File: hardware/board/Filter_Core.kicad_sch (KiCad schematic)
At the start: 53 parts

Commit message: Updated Prototype Tests
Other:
- note removed: "Notes:"
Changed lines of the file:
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@@
-    (effects (font (size 5 5) (thickness 0.508) bold) (justify left bottom))
-  )
-  (text "Notes:" (at 21.59 180.34 0)
     (effects (font (size 5 5) (thickness 0.508) bold) (justify left bottom))
   )

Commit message: hardware: add MPNs, DigiKey part numbers, and LCSC part numbers for all BOM items
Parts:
- C? (x7): DigiKey (none) -> 490-GCM1885C2A102FA16DCT-ND; LCSC (none) -> C2219251; MPN (none) -> GCM1885C2A102FA16D; Substitutes Allowed (none) -> Ask
- C? (x3): DigiKey (none) -> 1276-1008-1-ND; LCSC (none) -> C14858; MPN (none) -> CL10C101JB8NNNC; Rating 25V/10% -> 25V/10%/C0G; Substitutes Allowed (none) -> Yes
- D? (x12): DigiKey (none) -> 1727-4309-2-ND; LCSC (none) -> C109218; Substitutes Allowed (none) -> No
- R? (x7): DigiKey (none) -> YAG1582CT-ND; LCSC (none) -> C723637; MPN (none) -> RT0603BRD0720KL; Substitutes Allowed (none) -> Ask
- R? (x3): DigiKey (none) -> YAG2323TR-ND; LCSC (none) -> C375503; MPN (none) -> RT0603FRE071KL; Substitutes Allowed (none) -> Yes
- R?: DigiKey (none) -> YAG5959CT-ND; LCSC (none) -> C706162; MPN (none) -> RT0603FRE0733KL; Substitutes Allowed (none) -> Yes
- R?: DigiKey (none) -> 13-RT0603FRE13100KLTR-ND; LCSC (none) -> C4107493; MPN (none) -> RT0603FRE13100KL; Rating 100mW/1% -> 100mW/1%/Thin; Substitutes Allowed (none) -> Yes
- R?: DigiKey (none) -> 13-RT0603FRE07330KLCT-ND; LCSC (none) -> C863745; MPN (none) -> RT0603FRE07330KL; Rating 100mW/1% -> 100mW/1%/Thin; Substitutes Allowed (none) -> Yes
- R?: DigiKey (none) -> YAG5961CT-ND; LCSC (none) -> C863790; MPN (none) -> RT0603FRE073K9L; Substitutes Allowed (none) -> Yes
- R?: DigiKey (none) -> YAG1582CT-ND; LCSC (none) -> C723637; MPN (none) -> RT0603BRD0720KL; Rating 100mW/1%/Thin -> 100mW/0.1%/Thin; Substitutes Allowed (none) -> Ask
- R?: DigiKey (none) -> 13-RT0603FRE071K8LCT-ND; LCSC (none) -> C375505; MPN (none) -> RT0603FRE071K8L; Rating 100mW/1% -> 100mW/1%/Thin; Substitutes Allowed (none) -> Yes
- R? (x2): DigiKey (none) -> 13-RT0603FRE075K6LCT-ND; LCSC (none) -> C706186; MPN (none) -> RT0603FRE075K6L; Rating 100mW/1% -> 100mW/1%/Thin; Substitutes Allowed (none) -> Yes
- R?: DigiKey (none) -> YAG5967CT-ND; LCSC (none) -> C706189; MPN (none) -> RT0603FRE0768KL; Substitutes Allowed (none) -> Yes
- U? (x4): DigiKey (none) -> 296-7198-1-ND; LCSC (none) -> C96507; MPN TL074CPW -> TL074CPWR; Substitutes Allowed (none) -> No

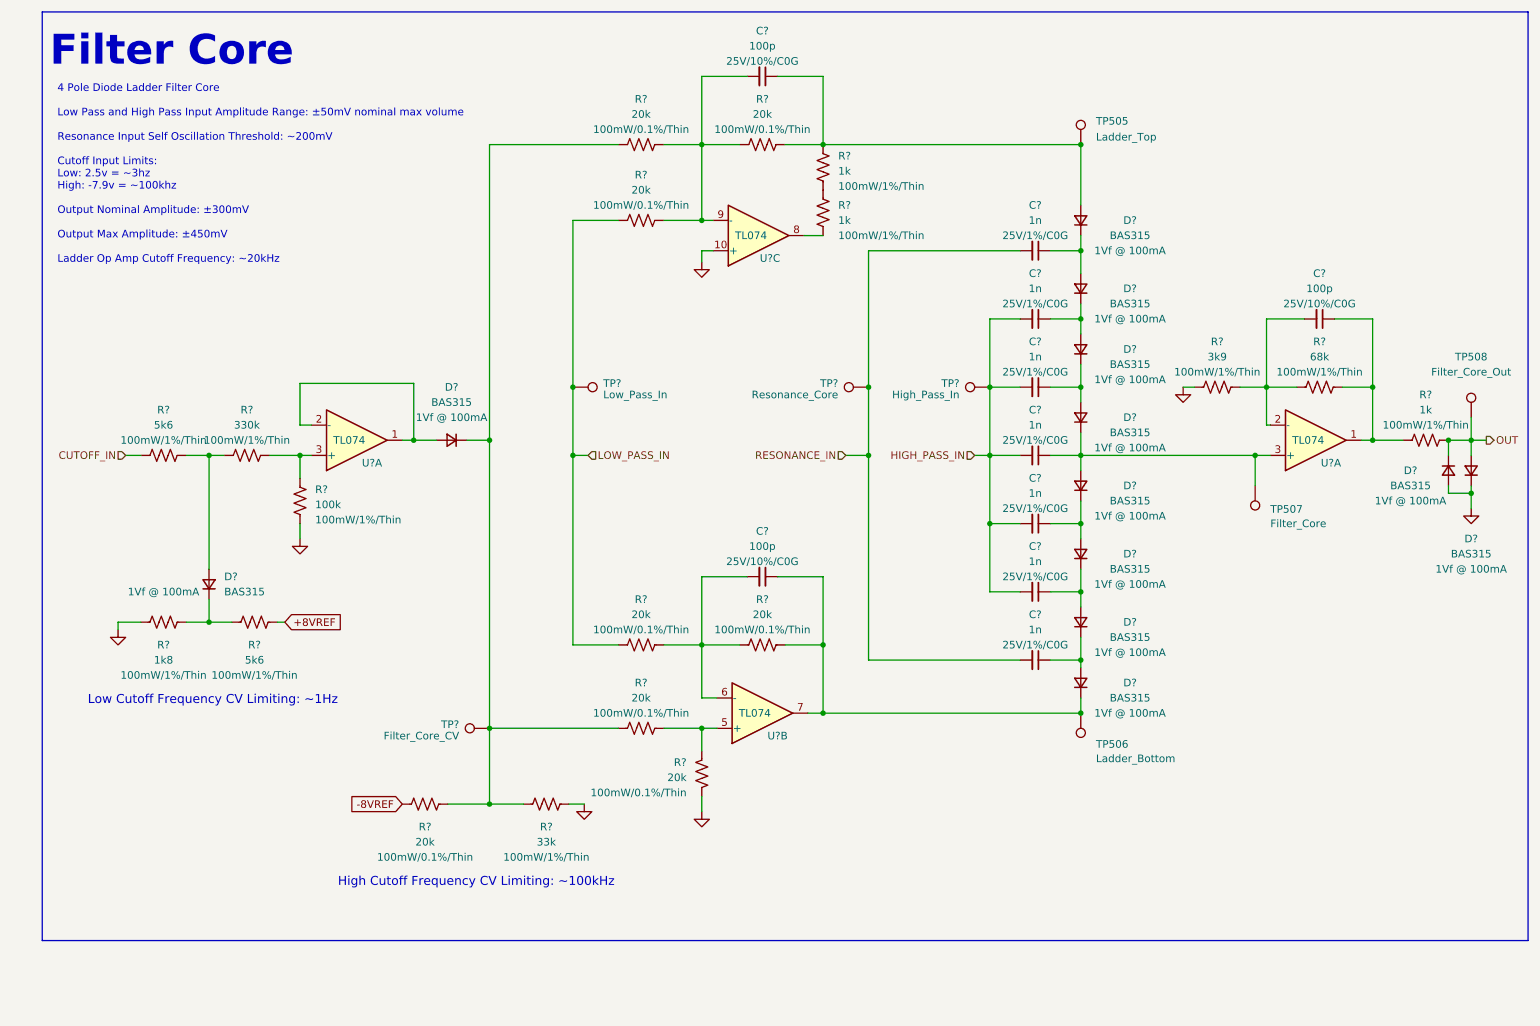
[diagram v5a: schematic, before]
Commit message: hardware: update schematic fonts/text sizes, some slight readability improvements
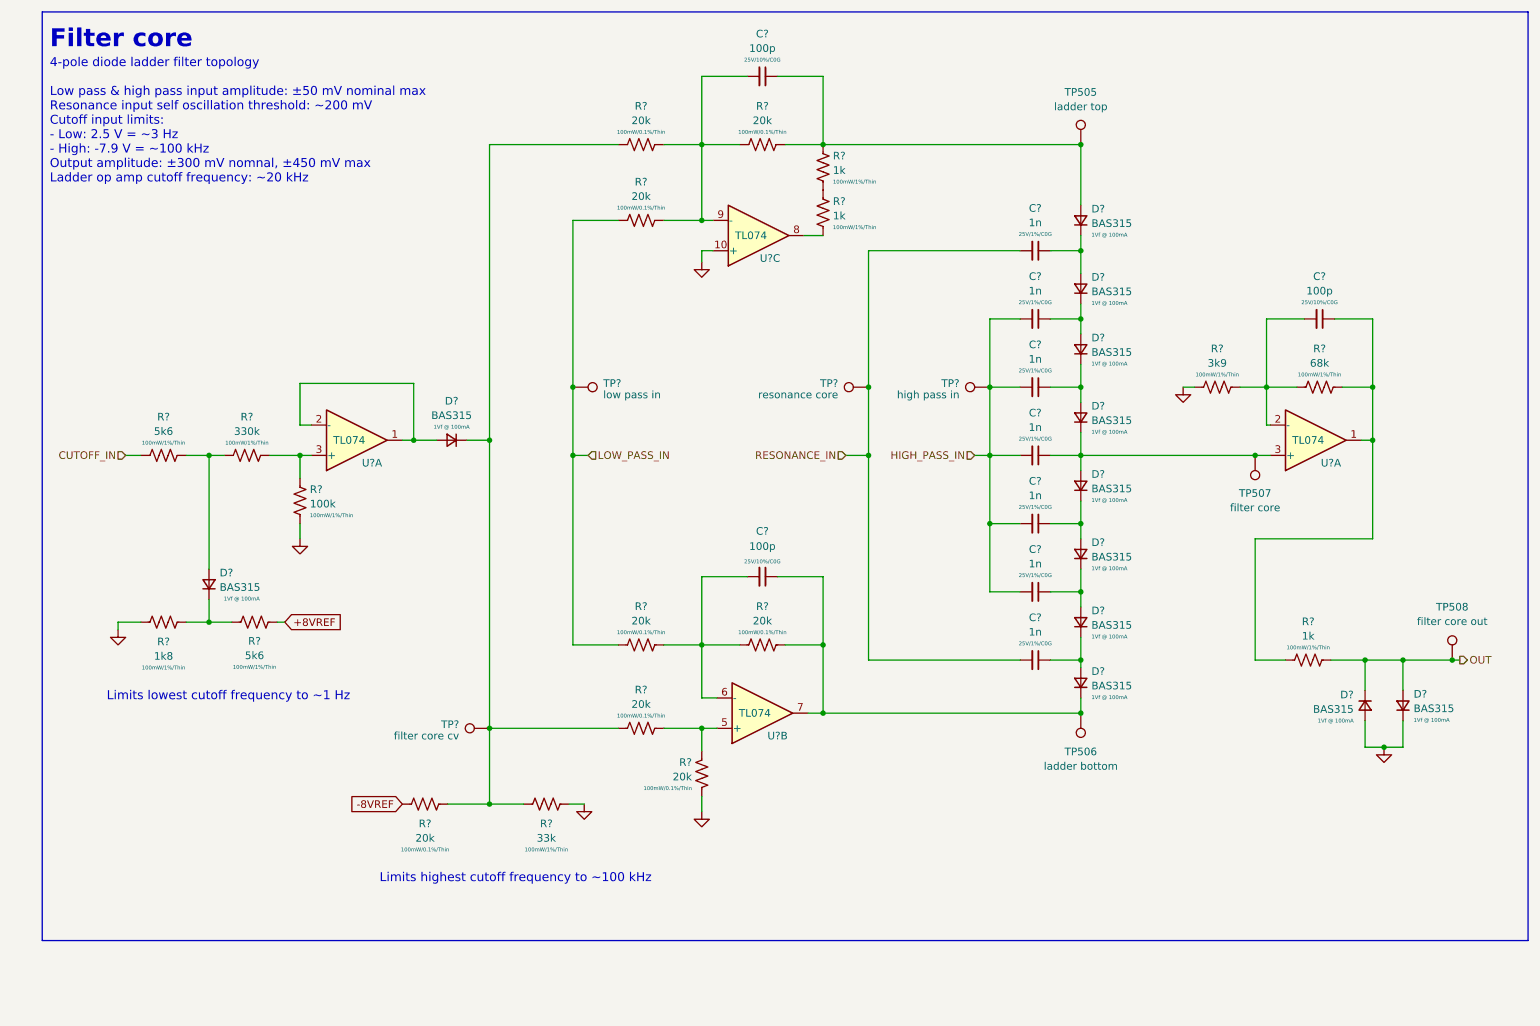
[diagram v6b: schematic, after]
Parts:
- TP505: Name Ladder_Top -> ladder top
- TP506: Name Ladder_Bottom -> ladder bottom
- TP507: Name Filter_Core -> filter core
- TP508: Name Filter_Core_Out -> filter core out
- TP?: Name Resonance_Core -> resonance core
- TP?: Name Low_Pass_In -> low pass in
- TP?: Name High_Pass_In -> high pass in
- TP?: Name Filter_Core_CV -> filter core cv
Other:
- note added: "4-pole diode ladder filter topology Low pass & high pass input amplitude: ±50 mV nominal max Resonance input self oscillation threshold: ~200 mV Cutoff input limits: - Low: 2.5 V = ~3 Hz - High: -7.9 V = ~100 kHz Output amplitude: ±300 mV nomnal, ±450 mV max Ladder op amp cutoff frequency: ~20 kHz"
- note added: "Filter core"
- note added: "Limits highest cutoff frequency to ~100 kHz"
- note added: "Limits lowest cutoff frequency to ~1 Hz"
- note removed: "4 Pole Diode Ladder Filter Core Low Pass and High Pass Input Amplitude Range: ±50mV nominal max volume Resonance Input Self Oscillation Threshold: ~200mV Cutoff Input Limits: Low: 2.5v = ~3hz High: -7.9v = ~100khz Output Nominal Amplitude: ±300mV Output Max Amplitude: ±450mV Ladder Op Amp Cutoff Frequency: ~20kHz"
- note removed: "Filter Core"
- note removed: "High Cutoff Frequency CV Limiting: ~100kHz"
- note removed: "Low Cutoff Frequency CV Limiting: ~1Hz"
- moved on the sheet: D?, R?, TP507, TP508

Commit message: hardware: use new Winterbloom sheet layout
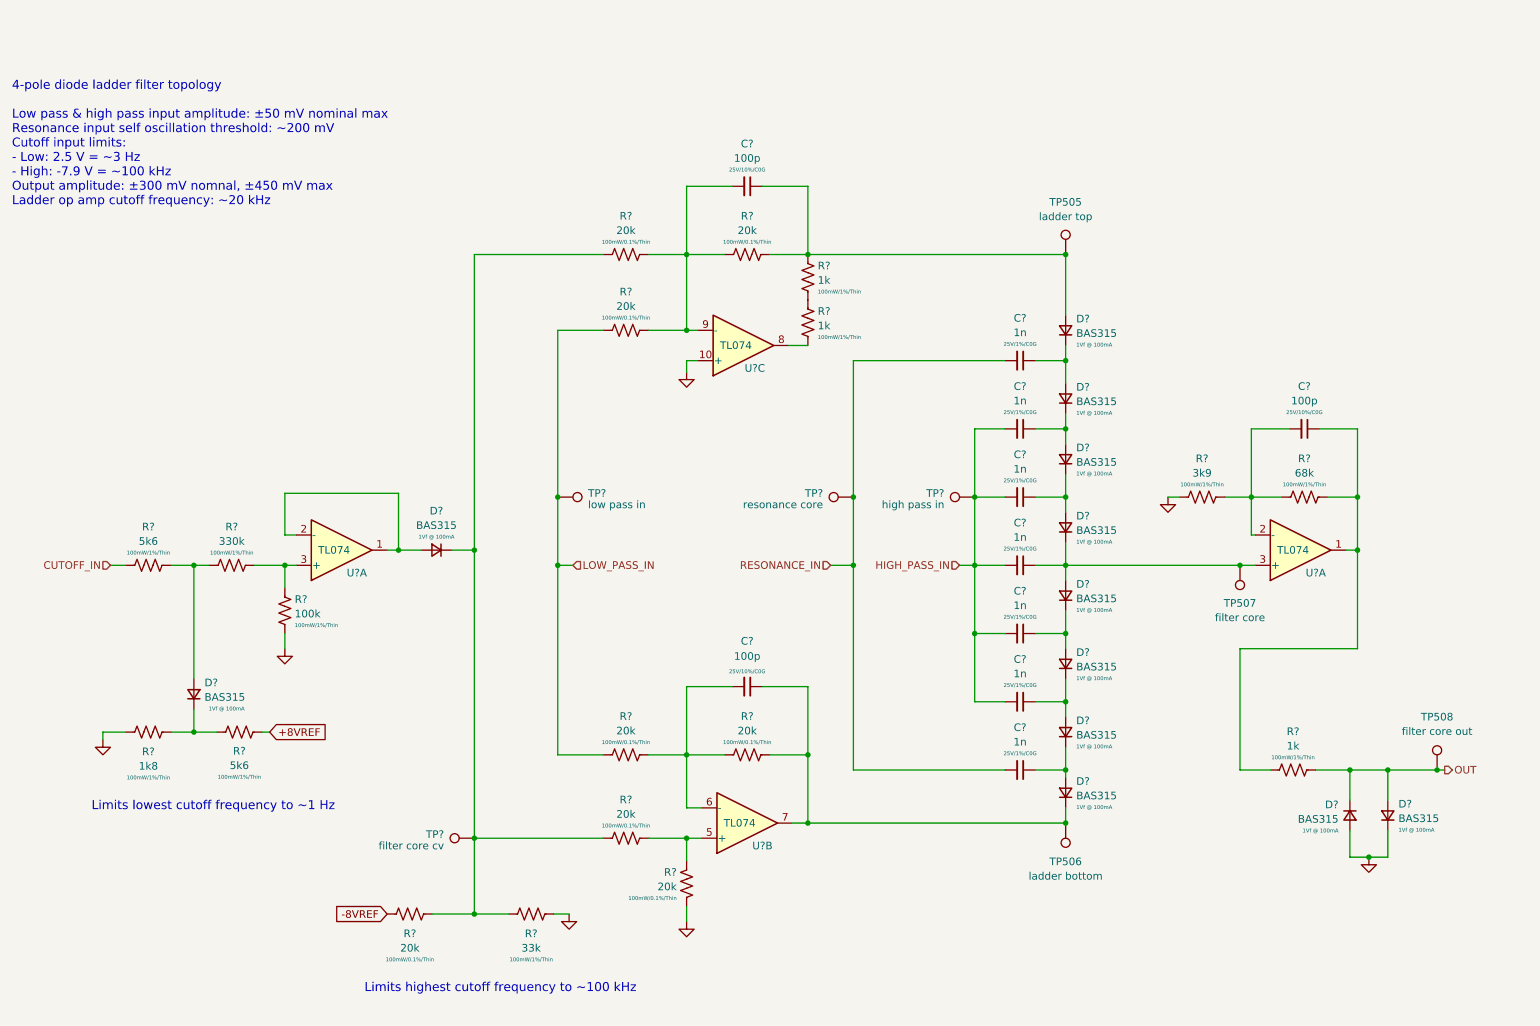
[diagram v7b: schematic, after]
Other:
- note removed: "Filter core"
- moved on the sheet: C?, D?, R?, TP505, TP506, TP507, TP508, TP?, U?A, U?B, U?C

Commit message: hardware: finalize v3
- Updated version number and release date
- Swapped TL074C to TL074H
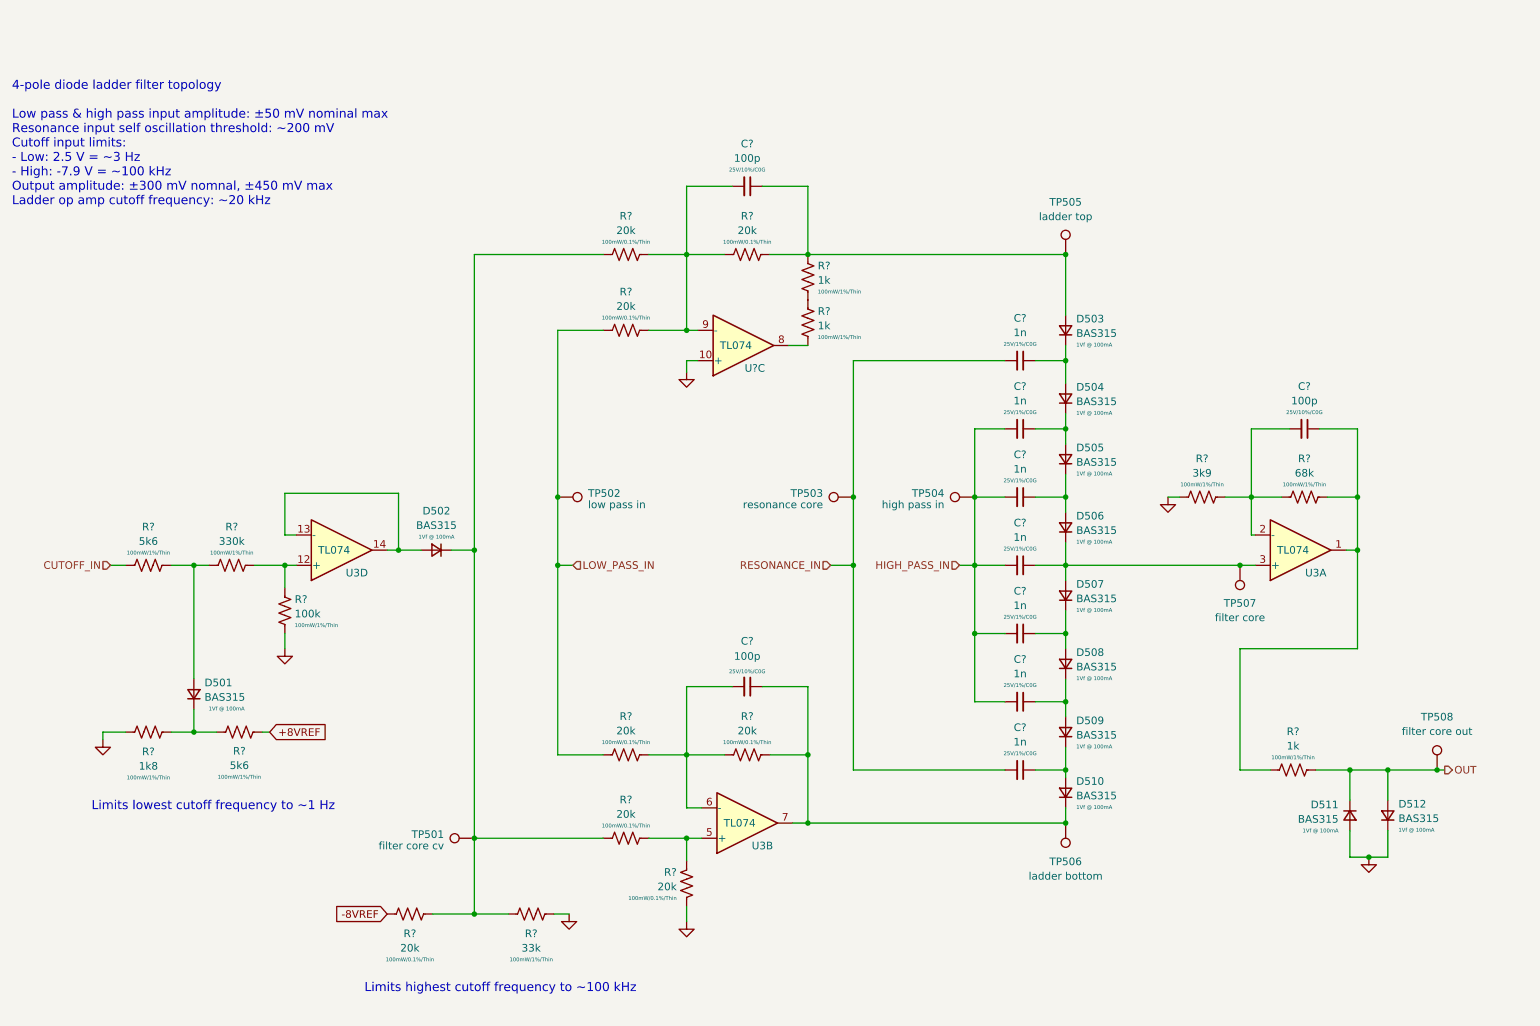
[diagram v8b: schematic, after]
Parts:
- U3: renamed from U?; DigiKey 296-7198-1-ND -> 296-TL074HIPWRCT-ND; LCSC C96507 -> C4370424; MPN TL074CPWR -> TL074HIPWR; Notes (none) -> TL074H over TL074C due to better input offset voltage
- U?: DigiKey 296-7198-1-ND -> 296-TL074HIPWRCT-ND; LCSC C96507 -> C4370424; MPN TL074CPWR -> TL074HIPWR; Notes (none) -> TL074H over TL074C due to better input offset voltage
- gave numbers to parts that had none: 16
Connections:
- net at R?.1, R?.1: now also U3.12 (+); no longer U3.3 (+)
- new net: D502.2 (A), U3.13 (-), U3.14
